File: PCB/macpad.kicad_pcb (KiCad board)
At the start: 2 copper layers, 61.9 x 81 mm, 23 parts, among them SW1 SW_Push, SW14 RotaryEncoder_Switch, SW15 RotaryEncoder_Switch, SW2 SW_Push, SW3 SW_Push, SW4 SW_Push, SW5 SW_Push, SW6 SW_Push, SW7 SW_Push, SW8 SW_Push, SW9 SW_Push, U1 XIAO-RP2040-DIP

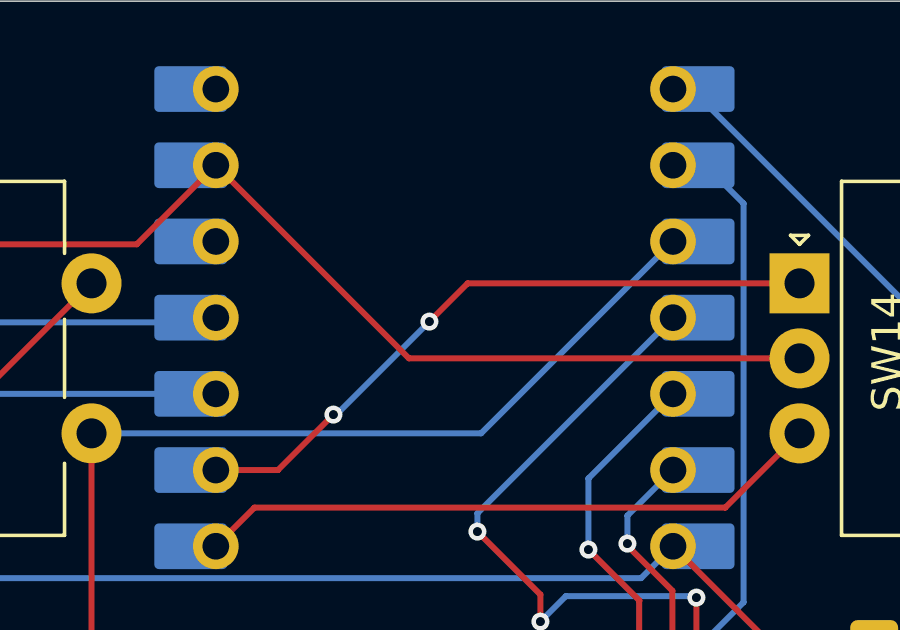
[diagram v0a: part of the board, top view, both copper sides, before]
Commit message: add silkscreen design
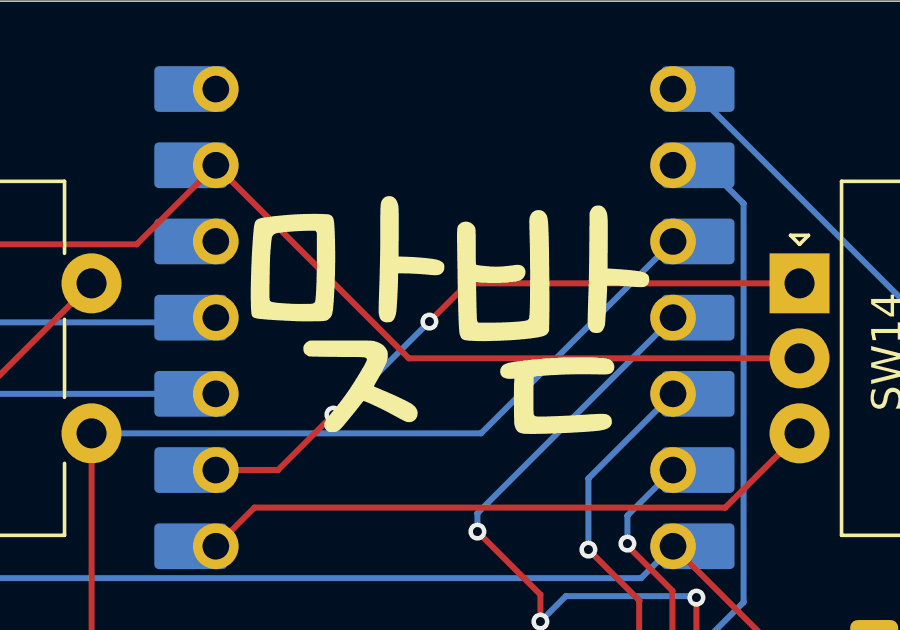
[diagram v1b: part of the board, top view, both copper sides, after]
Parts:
- added G***: LOGO, silkscreen_designs:korean_writing, F.Cu at (147.8, 84.3)
- added G***: LOGO, silkscreen_designs:macpad_writing, F.Cu at (147.9, 113.4)
